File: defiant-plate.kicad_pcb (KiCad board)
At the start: 2 copper layers, 126.1 x 99.6 mm, 28 parts, among them T0 SW_PUSH, T1 SW_PUSH, T2 SW_PUSH, T3 SW_PUSH, T4 SW_PUSH

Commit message: Experimental: Tighten thumb key placing
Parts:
- moved T4 0.99 mm to (191.4, 133.6)
- moved T3 0.80 mm to (172.6, 123.6)
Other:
- board size 126.1 x 99.6 mm -> 125.4 x 99.2 mm
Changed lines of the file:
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@@
   )
   (footprint "Defiant:SW_Gateron_LowProfile_Plate" (layer "F.Cu")
-    (at 192.333168 133.954069 -36)
+    (at 191.41961 133.562895 -36)
     (descr "Gateron Low Profile (KS-27 & KS-33) style mechanical keyboard switch, Gateron Low Profile hot-swap socket and through-hole soldering, the hole of the socket is plated, single-sided mounting. Gateron Low Profile and Cherry MX Low Profile are NOT compatible.")
     (tags "switch, low_profile, hot_swap")
@@
   )
   (footprint "Defiant:SW_Gateron_LowProfile_Plate" (layer "F.Cu")
-    (at 173.398584 123.880307 -20)
+    (at 172.64683 123.606691 -20)
     (descr "Gateron Low Profile (KS-27 & KS-33) style mechanical keyboard switch, Gateron Low Profile hot-swap socket and through-hole soldering, the hole of the socket is plated, single-sided mounting. Gateron Low Profile and Cherry MX Low Profile are NOT compatible.")
     (tags "switch, low_profile, hot_swap")
@@
   (gr_arc (start 174.264362 51.813324) (mid 175.678568 52.399114) (end 176.264362 53.813324)
     (stroke (width 0.1) (type default)) (layer "Edge.Cuts"))
-  (gr_line (start 161.844251 130.583323) (end 178.774251 136.713323)
+  (gr_line (start 161.844251 130.583323) (end 178.052037 136.45323)
     (stroke (width 0.1) (type default)) (layer "Edge.Cuts"))
   (gr_arc (start 160.771011 130.315765) (mid 161.317896 130.408369) (end 161.844251 130.583323)
@@
   (gr_line (start 143.384251 129.303322) (end 160.771011 130.315765)
     (stroke (width 0.1) (type default)) (layer "Edge.Cuts"))
-  (gr_arc (start 205.046042 130.406818) (mid 205.870563 131.722611) (end 205.523182 133.236042)
+  (gr_arc (start 204.275479 129.844207) (mid 205.1 131.16) (end 204.752619 132.673431)
     (stroke (width 0.1) (type default)) (layer "Edge.Cuts"))
   (gr_arc (start 195.269951 98.659951) (mid 194.684179 100.074179) (end 193.269951 100.659951)
@@
   (gr_line (start 193.27 100.65) (end 175.85 100.65)
     (stroke (width 0.1) (type default)) (layer "Edge.Cuts"))
-  (gr_line (start 205.046042 130.406818) (end 191.296753 120.563385)
+  (gr_line (start 204.275479 129.844207) (end 191.296753 120.563385)
     (stroke (width 0.1) (type default)) (layer "Edge.Cuts"))
   (gr_line (start 98.774252 53.813324) (end 98.774251 59.813323)
@@
   (gr_arc (start 98.774252 53.813324) (mid 99.360038 52.39911) (end 100.774252 51.813324)
     (stroke (width 0.1) (type default)) (layer "Edge.Cuts"))
-  (gr_arc (start 195.782279 146.628903) (mid 194.477115 147.428701) (end 192.988674 147.071366)
+  (gr_arc (start 194.870117 146.218857) (mid 193.564943 147.018681) (end 192.076512 146.66132)
     (stroke (width 0.1) (type default)) (layer "Edge.Cuts"))
   (gr_line (start 79.774251 61.813323) (end 79.774251 116.303323)
@@
   (gr_line (start 100.774252 129.303322) (end 143.384251 129.303322)
     (stroke (width 0.1) (type default)) (layer "Edge.Cuts"))
-  (gr_line (start 205.523182 133.236042) (end 195.782279 146.628903)
+  (gr_line (start 204.752619 132.673431) (end 194.870116 146.218833)
     (stroke (width 0.1) (type default)) (layer "Edge.Cuts"))
   (gr_line (start 190.210153 120.286479) (end 187.184214 120.31)
@@
   (gr_line (start 193.26427 61.203304) (end 176.264251 61.203304)
     (stroke (width 0.1) (type default)) (layer "Edge.Cuts"))
-  (gr_line (start 192.988674 147.071366) (end 178.774251 136.713323)
+  (gr_line (start 192.076512 146.66132) (end 178.052037 136.45323)
     (stroke (width 0.1) (type default)) (layer "Edge.Cuts"))
   (gr_arc (start 187.184214 120.31) (mid 185.77 119.724214) (end 185.184214 118.31)
@@
     (effects (font (size 1 1) (thickness 0.15)) (justify left bottom))
   )
+  (group "" (id 80c8c62c-9fcb-4d36-b24e-8b415d0671ae)
+    (members
+      00bf3f3e-b9d5-4964-8f21-674bc8874993
+      04572bb3-2238-4247-a8dd-3b13a789e49b
+      0fcea472-68b1-44c8-ac8d-77b0d9fa2038
+      137e6e71-51f5-490b-bcf5-38d57dbf122b
+      187880dd-dbe2-4f07-9fd4-3625e335b4af
+      1b6d2ddd-5e23-4b2f-8eb2-bbd8625d822b
+      1d862835-9a83-44e9-a4a0-118baa66f62e
+      26d3e322-20e0-4678-9fe2-7c2475af3b05
+      2907f11e-160f-4618-beb6-c4b8d875aff3
+      2ef10bcc-73e2-461e-97c1-eefc00f460ea
+      2f57fc79-a697-4788-95e9-1dab930f9fe4
+      3ecf6329-27cf-47be-9343-7aa17994766d
+      3f0822e6-73b7-49f4-bac1-605b2b248c26
+      41e2dbde-a439-40e1-bcd7-f6f599d7119c
+      42b800f3-1d83-4b55-9aad-cf2cad6d1635
+      50627230-a6c5-43fa-b095-e8d76ef6b16c
+      54d0a574-9f7d-4f7c-8c64-fdc0ca3e3258
+      57ea1219-470e-4400-b2e9-9a4d3fa6eb14
+      657e030a-431b-4145-aabd-bbb684768414
+      66c119ba-26b8-4680-b1a1-a54c32bab990
+      6d22f171-ca04-4436-bead-2aa30f1570a9
+      6f5c9bba-3061-40f5-9d11-c229c1d8b13d
+      82f5b0c4-158c-4037-ae77-8f41119a89a5
+      8d36f90a-d68c-4fa8-bdc4-4bb3faac0c2a
+      8ecc577c-01b8-442f-871c-9ae66f177b6b
+      9ceb8403-4be3-4063-8ecc-b1eaea6e793f
+      a6f6d37f-4fc6-4f31-8d9c-a2c1cc73ed61
+      ab194198-a741-481c-b59c-6c8ed288259b
+      ab233530-da3c-4273-8376-32f9629841c1
+      ab395b4b-0ee3-464b-be4b-27ac47187c30
+      b4fc6401-e446-4953-a472-ebde5c8b8d66
+      bb08e371-c793-4f6c-bc66-a24afb154a1f
+      c0b919f3-b047-4cb3-8561-e3c8630304c2
+      d211463e-9430-423f-89b0-754f99027c05
+      d90c28dc-664c-46a6-b702-f5e37777b307
+      d9f6b089-a5d5-4ed1-938c-463d85a0e7a5
+      da04bc08-2770-4f4c-a7d2-85dfcb33a628
+      ea6f10e5-2714-4943-8970-3adfed318d99
+      f9c48685-cabf-4918-b0c4-b06fd2c1c7a6
+    )
+  )
 )

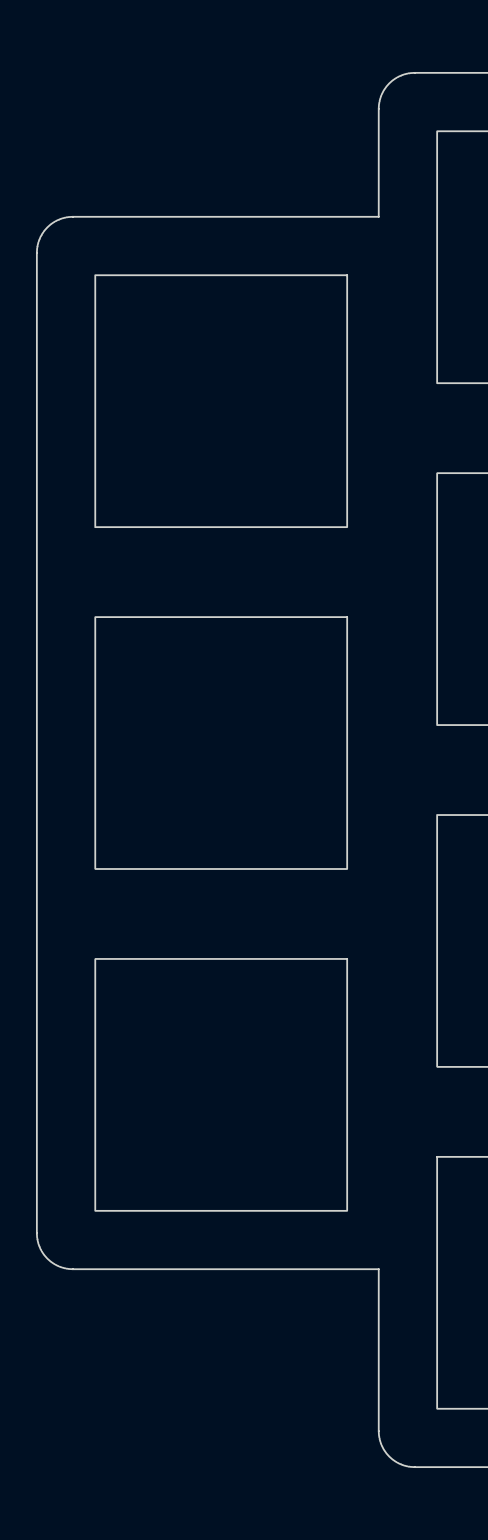
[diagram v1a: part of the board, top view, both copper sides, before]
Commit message: Move pinky column down by 1mm
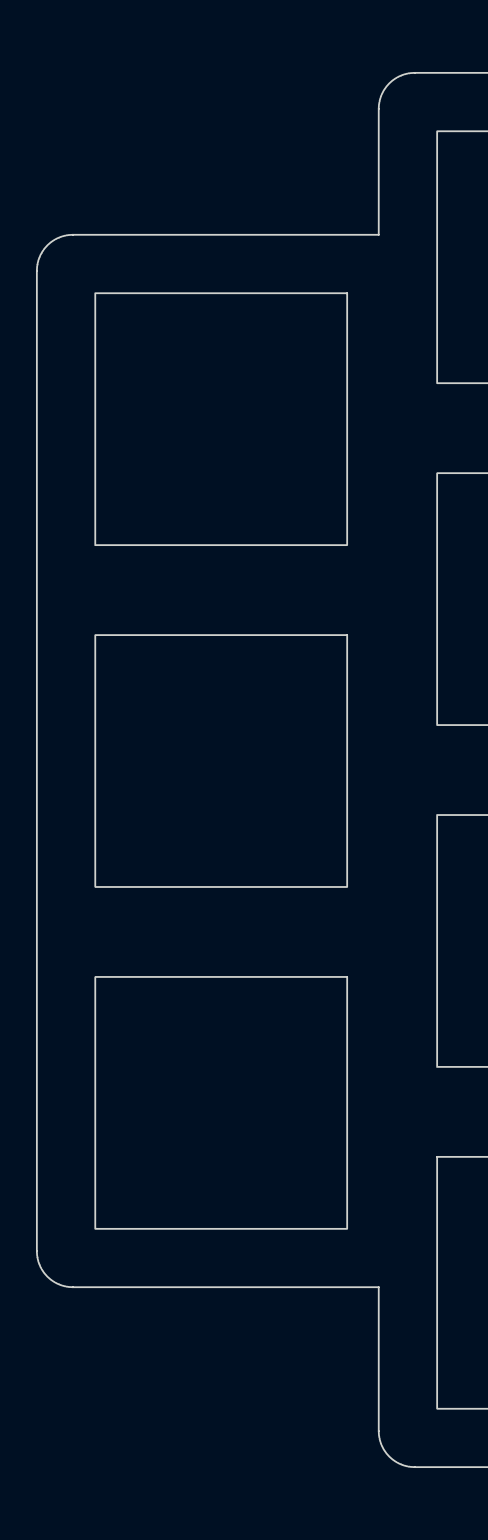
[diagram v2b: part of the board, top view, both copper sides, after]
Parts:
- moved C0R1 1.00 mm to (90.0, 71.1)
- moved C0R2 1.00 mm to (90.0, 90.1)
- moved C0R3 1.00 mm to (90.0, 109.1)
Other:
- outline, holes or cut-outs redrawn
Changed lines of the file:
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@@
   )
   (footprint "Defiant:SW_Gateron_LowProfile_Plate" (layer "B.Cu")
-    (at 90.018816 89.060447 180)
+    (at 90.018816 90.060447 180)
     (descr "Gateron Low Profile (KS-27 & KS-33) style mechanical keyboard switch, Gateron Low Profile hot-swap socket and through-hole soldering, the hole of the socket is plated, single-sided mounting. Gateron Low Profile and Cherry MX Low Profile are NOT compatible.")
     (tags "switch, low_profile, hot_swap")
@@
   )
   (footprint "Defiant:SW_Gateron_LowProfile_Plate" (layer "B.Cu")
-    (at 90.018816 70.060448 180)
+    (at 90.018816 71.060448 180)
     (descr "Gateron Low Profile (KS-27 & KS-33) style mechanical keyboard switch, Gateron Low Profile hot-swap socket and through-hole soldering, the hole of the socket is plated, single-sided mounting. Gateron Low Profile and Cherry MX Low Profile are NOT compatible.")
     (tags "switch, low_profile, hot_swap")
@@
   )
   (footprint "Defiant:SW_Gateron_LowProfile_Plate" (layer "B.Cu")
-    (at 90.018815 108.060447 180)
+    (at 90.018815 109.060447 180)
     (descr "Gateron Low Profile (KS-27 & KS-33) style mechanical keyboard switch, Gateron Low Profile hot-swap socket and through-hole soldering, the hole of the socket is plated, single-sided mounting. Gateron Low Profile and Cherry MX Low Profile are NOT compatible.")
     (tags "switch, low_profile, hot_swap")
@@
   (gr_line (start 204.275479 129.844207) (end 191.296753 120.563385)
     (stroke (width 0.1) (type default)) (layer "Edge.Cuts"))
-  (gr_line (start 98.774252 53.813324) (end 98.774251 59.813323)
-    (stroke (width 0.1) (type default)) (layer "Edge.Cuts"))
-  (gr_line (start 81.774251 59.813323) (end 98.774251 59.813323)
-    (stroke (width 0.1) (type default)) (layer "Edge.Cuts"))
-  (gr_line (start 98.774252 127.303322) (end 98.774252 118.303323)
+  (gr_line (start 98.774252 53.813324) (end 98.774251 60.813323)
+    (stroke (width 0.1) (type default)) (layer "Edge.Cuts"))
+  (gr_line (start 81.774251 60.813323) (end 98.774251 60.813323)
+    (stroke (width 0.1) (type default)) (layer "Edge.Cuts"))
+  (gr_line (start 98.774252 127.303322) (end 98.774252 119.303323)
     (stroke (width 0.1) (type default)) (layer "Edge.Cuts"))
   (gr_line (start 183.19 108.5) (end 175.85 108.5)
@@
   (gr_arc (start 100.774252 129.303322) (mid 99.360038 128.717536) (end 98.774252 127.303322)
     (stroke (width 0.1) (type default)) (layer "Edge.Cuts"))
-  (gr_arc (start 81.774251 118.303323) (mid 80.360037 117.717537) (end 79.774251 116.303323)
+  (gr_arc (start 81.774251 119.303323) (mid 80.359996 118.717556) (end 79.774251 117.303323)
     (stroke (width 0.1) (type default)) (layer "Edge.Cuts"))
   (gr_line (start 185.184214 118.31) (end 185.19 110.5)
@@
   (gr_arc (start 194.870117 146.218857) (mid 193.564943 147.018681) (end 192.076512 146.66132)
     (stroke (width 0.1) (type default)) (layer "Edge.Cuts"))
-  (gr_line (start 79.774251 61.813323) (end 79.774251 116.303323)
+  (gr_line (start 79.774251 62.813323) (end 79.774251 117.303323)
     (stroke (width 0.1) (type default)) (layer "Edge.Cuts"))
   (gr_line (start 100.774252 51.813324) (end 117.774252 51.813324)
@@
   (gr_line (start 174.264362 51.813324) (end 138.264251 51.813324)
     (stroke (width 0.1) (type default)) (layer "Edge.Cuts"))
-  (gr_arc (start 79.774251 61.813323) (mid 80.360037 60.399109) (end 81.774251 59.813323)
+  (gr_arc (start 79.774251 62.813323) (mid 80.360032 61.399113) (end 81.774251 60.813323)
     (stroke (width 0.1) (type default)) (layer "Edge.Cuts"))
   (gr_line (start 117.774252 49.813324) (end 117.774253 51.813324)
@@
   (gr_line (start 138.26425 49.813324) (end 138.26425 51.813323)
     (stroke (width 0.1) (type default)) (layer "Edge.Cuts"))
-  (gr_line (start 81.774251 118.303323) (end 98.774252 118.303323)
+  (gr_line (start 81.774251 119.303323) (end 98.774252 119.303323)
     (stroke (width 0.1) (type default)) (layer "Edge.Cuts"))
   (gr_arc (start 193.26427 61.203304) (mid 194.678478 61.789096) (end 195.26427 63.203304)
@@
     (effects (font (size 1 1) (thickness 0.15)) (justify left bottom))
   )
-  (group "" (id 80c8c62c-9fcb-4d36-b24e-8b415d0671ae)
-    (members
-      00bf3f3e-b9d5-4964-8f21-674bc8874993
-      04572bb3-2238-4247-a8dd-3b13a789e49b
-      0fcea472-68b1-44c8-ac8d-77b0d9fa2038
-      137e6e71-51f5-490b-bcf5-38d57dbf122b
-      187880dd-dbe2-4f07-9fd4-3625e335b4af
-      1b6d2ddd-5e23-4b2f-8eb2-bbd8625d822b
-      1d862835-9a83-44e9-a4a0-118baa66f62e
-      26d3e322-20e0-4678-9fe2-7c2475af3b05
-      2907f11e-160f-4618-beb6-c4b8d875aff3
-      2ef10bcc-73e2-461e-97c1-eefc00f460ea
-      2f57fc79-a697-4788-95e9-1dab930f9fe4
-      3ecf6329-27cf-47be-9343-7aa17994766d
-      3f0822e6-73b7-49f4-bac1-605b2b248c26
-      41e2dbde-a439-40e1-bcd7-f6f599d7119c
-      42b800f3-1d83-4b55-9aad-cf2cad6d1635
-      50627230-a6c5-43fa-b095-e8d76ef6b16c
-      54d0a574-9f7d-4f7c-8c64-fdc0ca3e3258
-      57ea1219-470e-4400-b2e9-9a4d3fa6eb14
-      657e030a-431b-4145-aabd-bbb684768414
-      66c119ba-26b8-4680-b1a1-a54c32bab990
-      6d22f171-ca04-4436-bead-2aa30f1570a9
-      6f5c9bba-3061-40f5-9d11-c229c1d8b13d
-      82f5b0c4-158c-4037-ae77-8f41119a89a5
-      8d36f90a-d68c-4fa8-bdc4-4bb3faac0c2a
-      8ecc577c-01b8-442f-871c-9ae66f177b6b
-      9ceb8403-4be3-4063-8ecc-b1eaea6e793f
-      a6f6d37f-4fc6-4f31-8d9c-a2c1cc73ed61
-      ab194198-a741-481c-b59c-6c8ed288259b
-      ab233530-da3c-4273-8376-32f9629841c1
-      ab395b4b-0ee3-464b-be4b-27ac47187c30
-      b4fc6401-e446-4953-a472-ebde5c8b8d66
-      bb08e371-c793-4f6c-bc66-a24afb154a1f
-      c0b919f3-b047-4cb3-8561-e3c8630304c2
-      d211463e-9430-423f-89b0-754f99027c05
-      d90c28dc-664c-46a6-b702-f5e37777b307
-      d9f6b089-a5d5-4ed1-938c-463d85a0e7a5
-      da04bc08-2770-4f4c-a7d2-85dfcb33a628
-      ea6f10e5-2714-4943-8970-3adfed318d99
-      f9c48685-cabf-4918-b0c4-b06fd2c1c7a6
-    )
-  )
 )
